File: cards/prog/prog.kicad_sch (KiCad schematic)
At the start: 121 parts, among them J1 BUS, J2 P7, J3 P6, J4 P5, J5 P4, J6 G3, J7 G2, Q1 2N7000, Q10 2N7000, Q11 2N7000, Q12 2N7000, Q13 2N7000, Q14 2N7000, Q15 2N7000, Q16 2N7000, Q17 2N7000, Q18 2N7000, Q19 2N7000, Q2 2N7000, Q20 2N7000, Q21 2N7000, Q22 2N7000, Q23 2N7000, Q24 2N7000, Q25 2N7000, Q26 2N7000, Q27 2N7000, Q28 2N7000, Q29 2N7000, Q3 2N7000, Q30 2N7000, Q31 2N7000, Q32 2N7000, Q33 2N7000, Q34 2N7000, Q35 2N7000, Q36 2N7000, Q37 2N7000, Q38 2N7000, Q39 2N7000, Q4 2N7000, Q40 2N7000, Q41 2N7000, Q5 2N7000, Q6 2N7000, Q7 2N7000, Q8 2N7000, Q9 2N7000, SW1 WORD 0, SW2 WORD 1, SW3 WORD 2, SW4 WORD 3

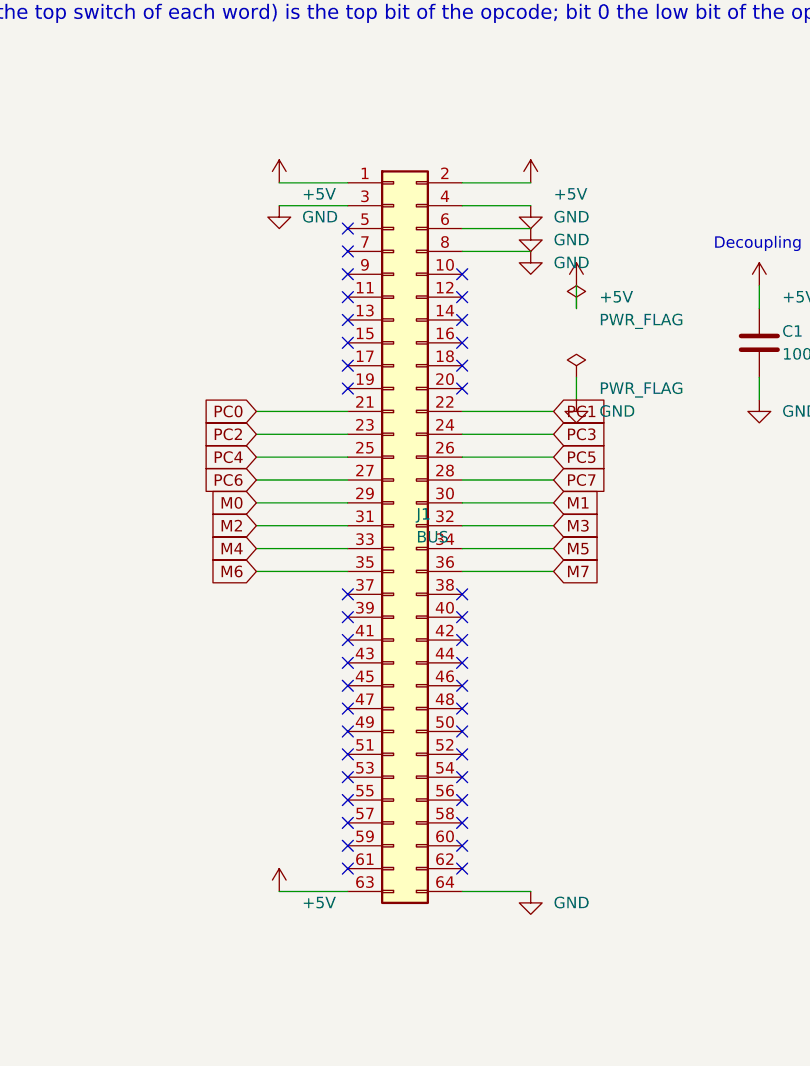
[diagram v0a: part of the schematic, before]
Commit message: The bus headers go on the back of all 26 boards, no track moved; the silkscreen refitted (D059, D062)
An IDC socket lies across its ribbon, so the ribbon could never run along a
row of cards as drawn. It runs behind them, and the 64-pin headers are
soldered on the back. This commit is that move, made in place on the routed
boards: no board was routed again.

How the header sits (D062): in the holes it had, turned over top to bottom,
notch toward the top edge. A pin of the odd row is then in the hole its even
neighbour had, so the two signals of every pair of pins change places: CLK
is pin 6, RST pin 8, +5V pins 1, 2 and 64. bus.py keeps both tables: PINS,
what the header's pins carry, and HOLES, what the copper was routed to.

The proof, on all 26 boards against 992a90f (sim/board_diff.py):
  netlist the same, element for element; every track, every via and every
  hole the same; each copper and mask layer differs by two pad shapes per
  header (pin 1's square went to the hole beside it, both on +5V) and the
  ground pour's outline round those two pads, nowhere else by more than a
  tenth of a micrometre.
sim/rebuild_check.py runs every builder into a scratch directory: each
writes the plan and the netlist that are committed, so a rebuild gives
this board. order_check.py --machine holds every pad of the 27 headers to
bus.py and requires them on the back.

What the move costs: on the ribbon RST had a ground conductor on both
sides; now one neighbour is BUS1#. tb_rst_neighbour.py puts the two lines
on the bench with every gate the routed boards hang on them: RST rises
0.28 to 0.43 V when BUS1# is released, against a lowest threshold of 0.8 V
(sim/results/rst_neighbour.md). The machine deck's crosstalk option now
couples the pins that are neighbours on the ribbon; the crosstalk stage of
the machine gate has to be run again on that order.

Silkscreen (pcb.fit_silk): every label to 1.0 mm where it has room, off
pads, vias, outlines and other labels, out from under the pa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
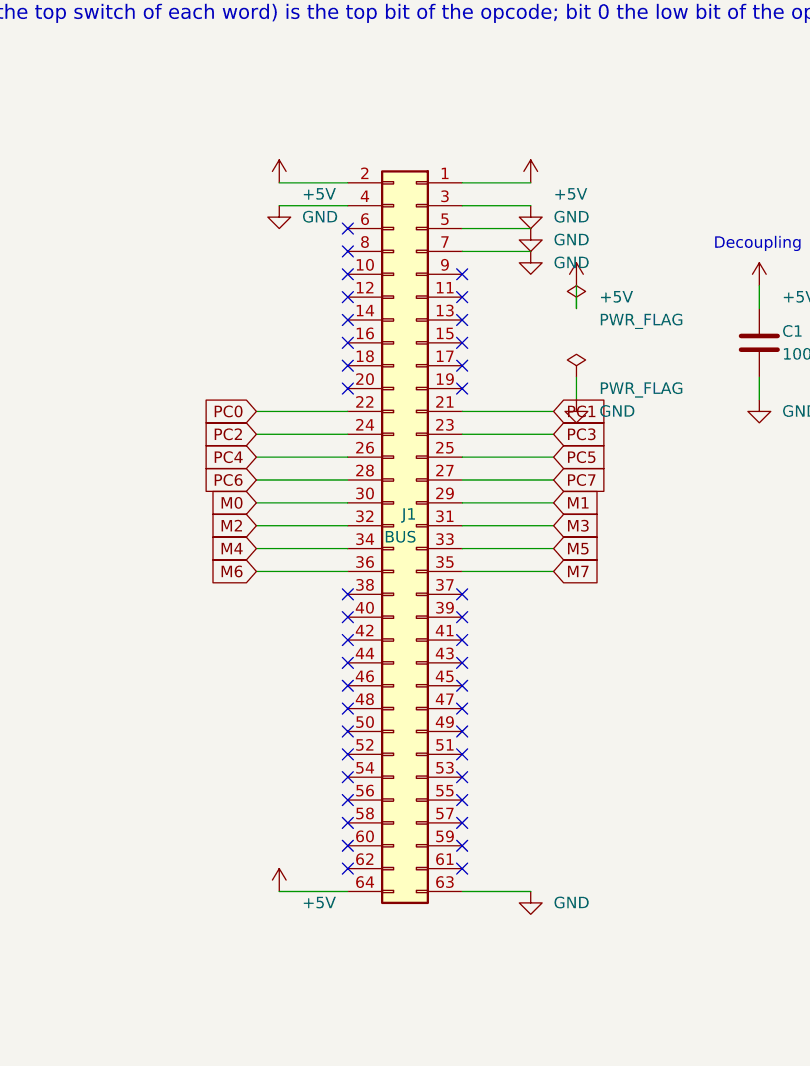
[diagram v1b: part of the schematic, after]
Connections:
- net +5V: now also J1.64 (Pin_64); no longer J1.63 (Pin_63)
- net GND: now also J1.5 (Pin_5), J1.63 (Pin_63), J1.7 (Pin_7); no longer J1.6 (Pin_6), J1.64 (Pin_64), J1.8 (Pin_8)
- net M0: now also J1.30 (Pin_30); no longer J1.29 (Pin_29)
- net M1: now also J1.29 (Pin_29); no longer J1.30 (Pin_30)
- net M2: now also J1.32 (Pin_32); no longer J1.31 (Pin_31)
- net M3: now also J1.31 (Pin_31); no longer J1.32 (Pin_32)
- net M4: now also J1.34 (Pin_34); no longer J1.33 (Pin_33)
- net M5: now also J1.33 (Pin_33); no longer J1.34 (Pin_34)
- net M6: now also J1.36 (Pin_36); no longer J1.35 (Pin_35)
- net M7: now also J1.35 (Pin_35); no longer J1.36 (Pin_36)
- net PC0: now also J1.22 (Pin_22); no longer J1.21 (Pin_21)
- net PC1: now also J1.21 (Pin_21); no longer J1.22 (Pin_22)
- net PC2: now also J1.24 (Pin_24); no longer J1.23 (Pin_23)
- net PC3: now also J1.23 (Pin_23); no longer J1.24 (Pin_24)
- net PC4: now also J1.26 (Pin_26); no longer J1.25 (Pin_25)
- net PC5: now also J1.25 (Pin_25); no longer J1.26 (Pin_26)
- net PC6: now also J1.28 (Pin_28); no longer J1.27 (Pin_27)
- net PC7: now also J1.27 (Pin_27); no longer J1.28 (Pin_28)
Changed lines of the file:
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@@
 	(symbol
 		(lib_id "Connector_Generic:Conn_02x32_Odd_Even")
-		(at 76.2 101.6 0)
+		(at 78.74 101.6 0)
+		(mirror y)
 		(unit 1)
 		(body_style 1)
